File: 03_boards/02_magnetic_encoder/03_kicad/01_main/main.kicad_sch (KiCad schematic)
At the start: 0 parts

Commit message: Finished Draft Linear Motor Encoder Schematic & Moved metric.ut to root for easier access across the repo
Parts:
- added C1, C3: 100nF, Capacitor_SMD:C_01005_0402Metric, symbol Device:C_Small
- added C2: 10uF, Capacitor_SMD:C_0201_0603Metric, symbol Device:C_Small
- added J1: 01x05, symbol Connector_Generic:Conn_01x05
- added U1: AS5311-ATST-500, TSSOP20_AS5311-ATST-500_AMS, symbol AS5311:AS5311-ATST-500
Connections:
- new net +3.3V: C2.1, C3.1, J1.1 (Pin_1), U1.18 (VDD3V3), U1.19 (VDD5V)
- new net GND: C1.1, C1.2, C2.2, C3.2, J1.5 (Pin_5), U1.14 (CSN), U1.8 (VSS), U1.9 (PROG)
- new net INA: J1.2 (Pin_2), U1.4 (A)
- new net INB: J1.3 (Pin_3), U1.5 (B)
- new net INX: J1.4 (Pin_4), U1.7 (INDEX)
- no-connect marks 0 -> 5
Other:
- note added: "Armature Connection"
- note added: "Incremental Magnetic Linear Encoder"
- title: (none) -> Linear Magnetic Encoder

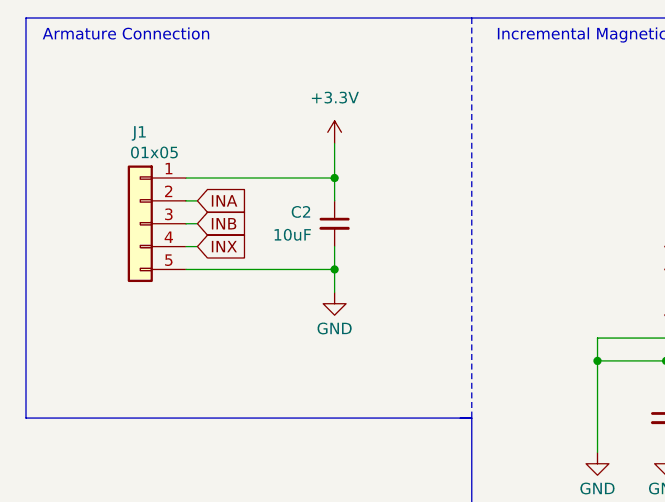
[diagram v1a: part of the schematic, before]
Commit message: Finished Validation & PCB for Magnetic Encoder Board
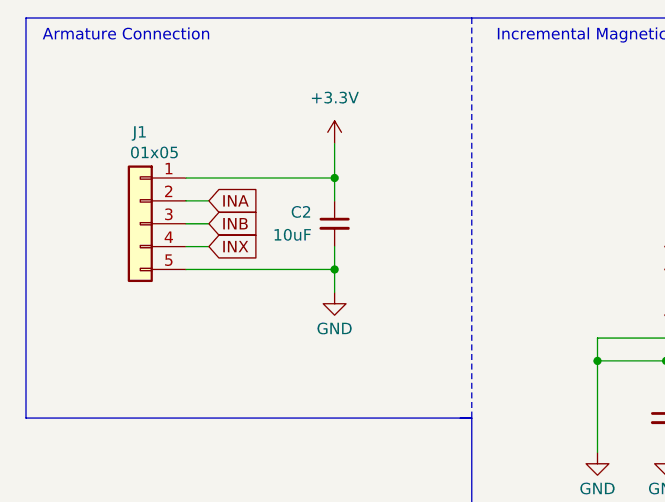
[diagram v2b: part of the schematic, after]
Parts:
- C1, C3: footprint Capacitor_SMD:C_01005_0402Metric -> Capacitor_SMD:C_0402_1005Metric; KiLib_Generator (none) -> SMD_2terminal_chip_molded
- C2: footprint Capacitor_SMD:C_0201_0603Metric -> Capacitor_SMD:C_1206_3216Metric; KiLib_Generator (none) -> SMD_2terminal_chip_molded
- J1: footprint (none) -> Connector_JST:JST_XA_B05B-XASK-1_1x05_P2.50mm_Vertical
- U1: footprint TSSOP20_AS5311-ATST-500_AMS -> AS5311:TSSOP20_AS5311-ATST-500_AMS

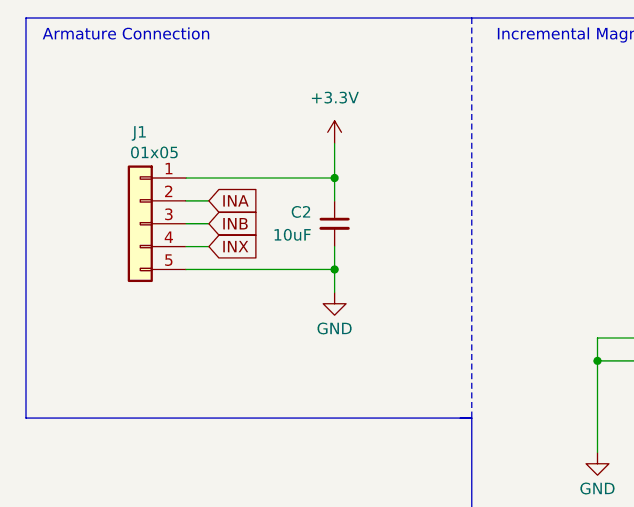
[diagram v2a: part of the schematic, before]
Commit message: Updated PCB for better mounting & also renamed reference in motor driver.
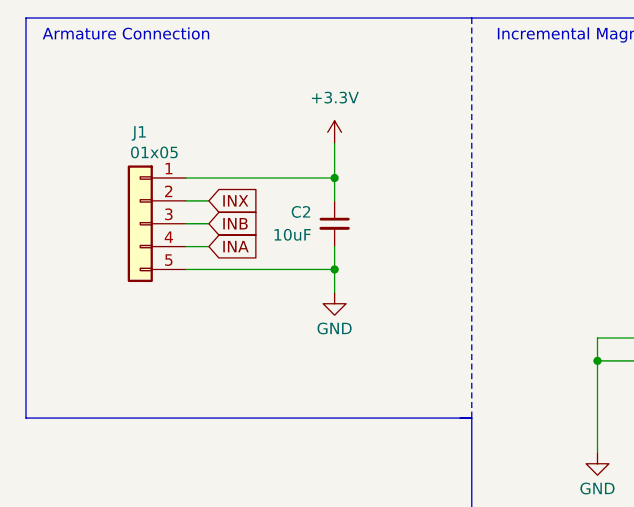
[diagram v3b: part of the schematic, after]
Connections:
- net INA: now also J1.4 (Pin_4); no longer J1.2 (Pin_2)
- net INX: now also J1.2 (Pin_2); no longer J1.4 (Pin_4)
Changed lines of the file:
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@@
+	(wire
+		(pts
+			(xy 156.21 36.83) (xy 156.21 31.75)
+		)
+		(stroke
+			(width 0)
+			(type default)
+		)
+	)
+	(wire
+		(pts
+			(xy 34.29 41.91) (xy 36.83 41.91)
+		)
+		(stroke
+			(width 0)
+			(type default)
+		)
+	)
 	(wire
 		(pts
@@
 	(wire
 		(pts
-			(xy 156.21 36.83) (xy 156.21 31.75)
-		)
-		(stroke
-			(width 0)
-			(type default)
-		)
-	)
-	(wire
-		(pts
 			(xy 156.21 39.37) (xy 156.21 36.83)
 		)
@@
 		(pts
 			(xy 16.51 60.96) (xy 66.04 60.96)
-		)
-		(stroke
-			(width 0)
-			(type default)
-		)
-	)
-	(wire
-		(pts
-			(xy 36.83 41.91) (xy 34.29 41.91)
 		)
 		(stroke
@@
 	(global_label "INA"
 		(shape input)
-		(at 36.83 36.83 0)
+		(at 36.83 41.91 0)
 		(fields_autoplaced yes)
 		(effects
@@
 		)
 		(property "Intersheetrefs" "${INTERSHEET_REFS}"
-			(at 42.8391 36.83 0)
+			(at 42.8391 41.91 0)
 			(hide yes)
 			(show_name no)
@@
 	(global_label "INX"
 		(shape input)
-		(at 36.83 41.91 0)
+		(at 36.83 36.83 0)
 		(fields_autoplaced yes)
 		(effects
@@
 		)
 		(property "Intersheetrefs" "${INTERSHEET_REFS}"
-			(at 42.96 41.91 0)
+			(at 42.96 36.83 0)
 			(hide yes)
 			(show_name no)

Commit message: Improvement Mounting & Added note on CL
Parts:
- added R1: 0Ω, Resistor_SMD:R_0402_1005Metric, symbol Device:R_Small
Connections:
- net GND: now also R1.1; no longer C1.1, U1.9 (PROG)
- new net: C1.1, R1.2, U1.9 (PROG)
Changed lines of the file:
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@@
+	)
+	(junction
+		(at 87.63 54.61)
+		(diameter 0)
+		(color 0 0 0 0)
 	)
 	(junction
@@
 		(color 0 0 0 0)
 	)
-	(junction
-		(at 87.63 54.61)
-		(diameter 0)
-		(color 0 0 0 0)
-	)
 	(no_connect
 		(at 143.51 52.07)
@@
 	(wire
 		(pts
-			(xy 80.01 64.77) (xy 80.01 54.61)
-		)
-		(stroke
-			(width 0)
-			(type default)
-		)
-	)
-	(wire
-		(pts
 			(xy 87.63 54.61) (xy 87.63 58.42)
 		)
@@
 	(wire
 		(pts
+			(xy 86.36 54.61) (xy 87.63 54.61)
+		)
+		(stroke
+			(width 0)
+			(type default)
+		)
+	)
+	(wire
+		(pts
 			(xy 50.8 30.48) (xy 50.8 34.29)
 		)
@@
 	(wire
 		(pts
-			(xy 80.01 54.61) (xy 87.63 54.61)
-		)
-		(stroke
-			(width 0)
-			(type default)
-		)
-	)
-	(wire
-		(pts
-			(xy 80.01 54.61) (xy 80.01 52.07)
+			(xy 80.01 52.07) (xy 80.01 54.61)
+		)
+		(stroke
+			(width 0)
+			(type default)
+		)
+	)
+	(wire
+		(pts
+			(xy 80.01 54.61) (xy 81.28 54.61)
+		)
+		(stroke
+			(width 0)
+			(type default)
+		)
+	)
+	(wire
+		(pts
+			(xy 80.01 54.61) (xy 80.01 64.77)
 		)
 		(stroke
@@
 					(unit 1)
 				)
+			)
+		)
+	)
+	(symbol
+		(lib_id "Device:R_Small")
+		(at 83.82 54.61 90)
+		(unit 1)
+		(body_style 1)
+		(exclude_from_sim no)
+		(in_bom yes)
+		(on_board yes)
+		(in_pos_files yes)
+		(dnp no)
+		(property "Reference" "R1"
+			(at 82.804 56.388 90)
+			(hide yes)
+			(show_name no)
+			(do_not_autoplace no)
+			(effects
+				(font
+					(size 1.016 1.016)
+				)
+			)
+		)
+		(property "Value" "0Ω"
+			(at 83.7351 54.6298 90)
+			(show_name no)
+			(do_not_autoplace no)
+			(effects
+				(font
+					(size 0.762 0.762)
+				)
+			)
+		)
+		(property "Footprint" "Resistor_SMD:R_0402_1005Metric"
+			(at 83.82 54.61 0)
+			(hide yes)
+			(show_name no)
+			(do_not_autoplace no)
+			(effects
+				(font
+					(size 1.27 1.27)
+				)
+			)
+		)
+		(property "Datasheet" ""
+			(at 83.82 54.61 0)
+			(hide yes)
+			(show_name no)
+			(do_not_autoplace no)
+			(effects
+				(font
+					(size 1.27 1.27)
+				)
+			)
+		)
+		(property "Description" "Resistor, small symbol"
+			(at 83.82 54.61 0)
+			(hide yes)
+			(show_name no)
+			(do_not_autoplace no)
+			(effects
+				(font
+					(size 1.27 1.27)
+				)
+			)
+		)
+		(pin "2"
+		)
+		(pin "1"
+		)
+		(instances
+			(project "main"
+				(path "/a09cebf3-5c51-433e-81aa-a6eac41f2816"
+					(reference "R1")
+					(unit 1)
+				)

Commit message: Updated Encoder KiCAD and removed actuation_comparsion
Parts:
- J1: footprint Connector_JST:JST_XA_B05B-XASK-1_1x05_P2.50mm_Vertical -> Connector_JST:JST_XH_B5B-XH-A_1x05_P2.50mm_Vertical
- U1: footprint AS5311:TSSOP20_AS5311-ATST-500_AMS -> footprints:TSSOP20_AS5311-ATST-500_AMS
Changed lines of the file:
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@@
 			)
 		)
-		(property "Footprint" "AS5311:TSSOP20_AS5311-ATST-500_AMS"
+		(property "Footprint" "footprints:TSSOP20_AS5311-ATST-500_AMS"
 			(at 92.71 34.29 0)
 			(hide yes)
@@
 			)
 		)
-		(property "Footprint" "Connector_JST:JST_XA_B05B-XASK-1_1x05_P2.50mm_Vertical"
+		(property "Footprint" "Connector_JST:JST_XH_B5B-XH-A_1x05_P2.50mm_Vertical"
 			(at 29.21 39.37 0)
 			(hide yes)
